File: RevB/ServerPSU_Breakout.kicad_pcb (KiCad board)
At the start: 2 copper layers, 124 x 100 mm, 81 parts, among them J1 Conn_01x05, J2 Conn_01x14, J3 Conn_01x01, J4 Conn_01x01, Q1 DMG2302U, SW1 SW_DIP_x03, SW2 SW_DIP_x04, SW3 SW_DIP_x03, U1 LMR14206, U2 STM32F072RBTx, U3 4051, U4 MIC1555-YM5, U6 MCP1415, U7 AZ1117CR-3.3

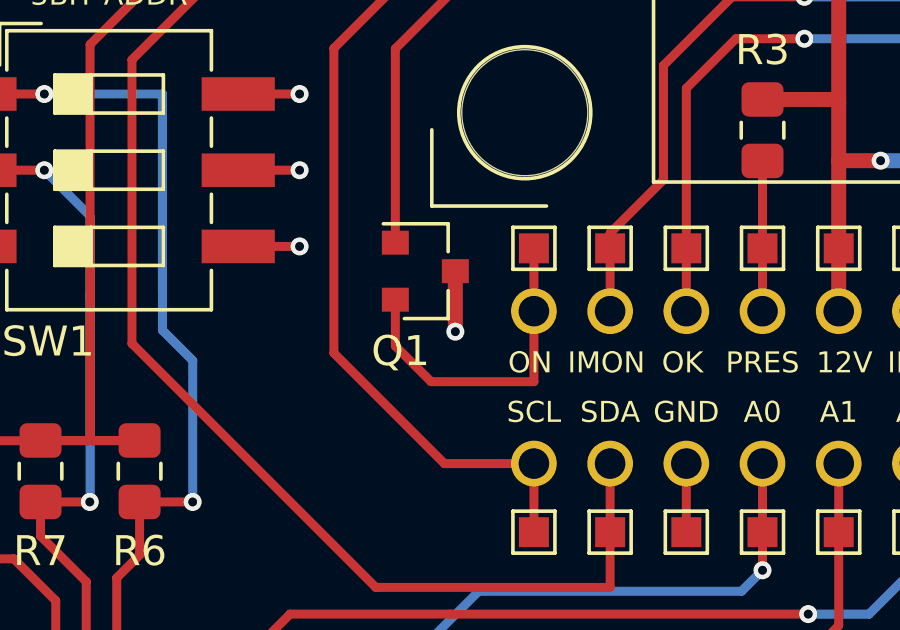
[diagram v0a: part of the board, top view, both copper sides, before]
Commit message: update RevB design
- Corrected PSU_ON n-chan. Drain and Source swapped.
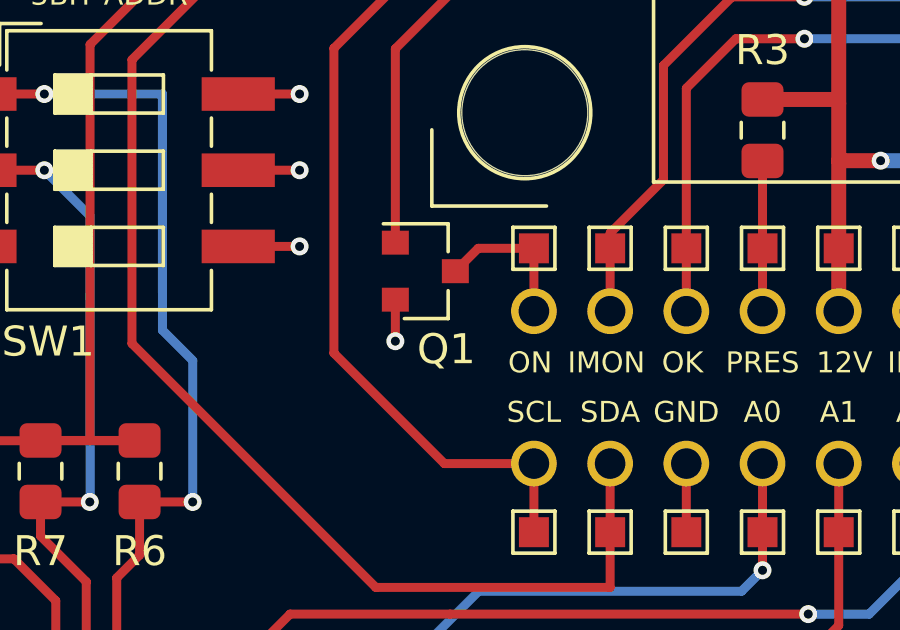
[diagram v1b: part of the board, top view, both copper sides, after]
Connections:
- Q1 pad 2: /HighVoltageControl/PSU_ON -> GNDS
- Q1 pad 3: GNDS -> /HighVoltageControl/PSU_ON
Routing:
- net /HighVoltageControl/PSU_ON: track 11.1 -> 5.03 mm
- net GNDS: track 76.9 -> 76.3 mm

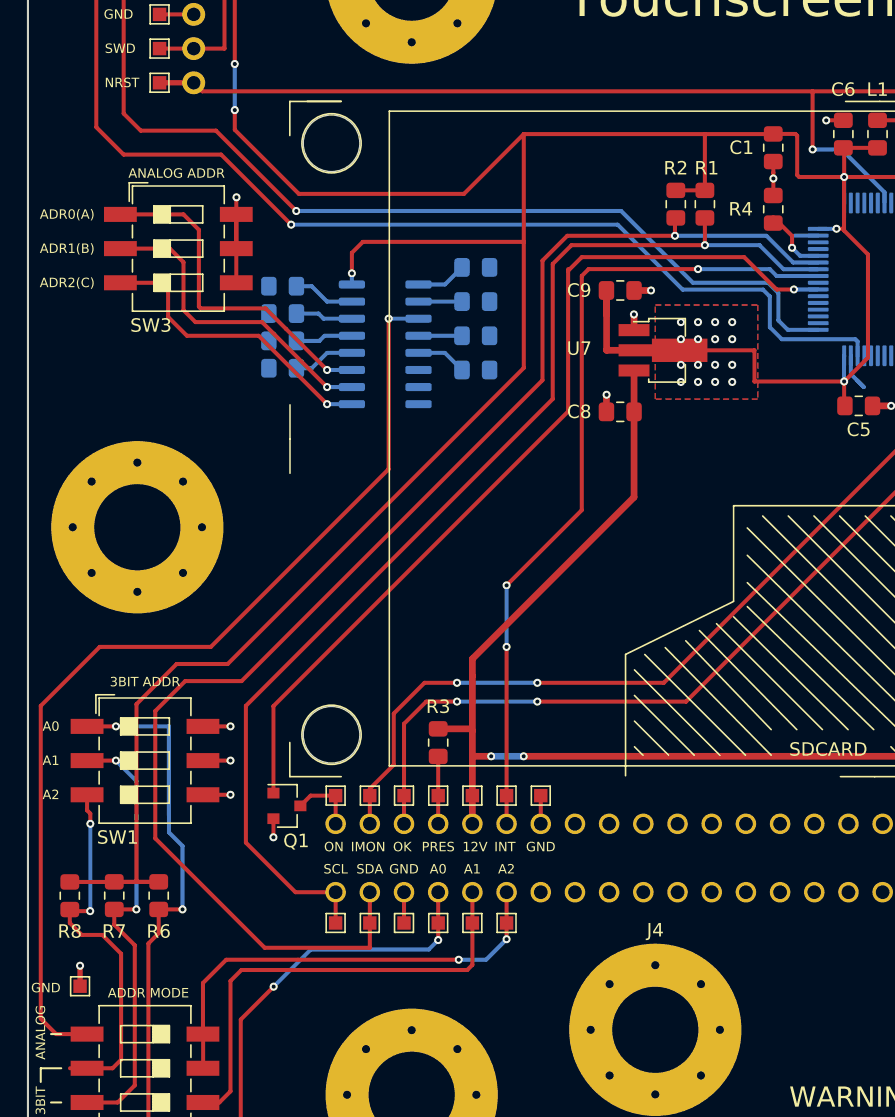
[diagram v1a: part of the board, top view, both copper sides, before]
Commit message: updated revb
added missing pullup resistors
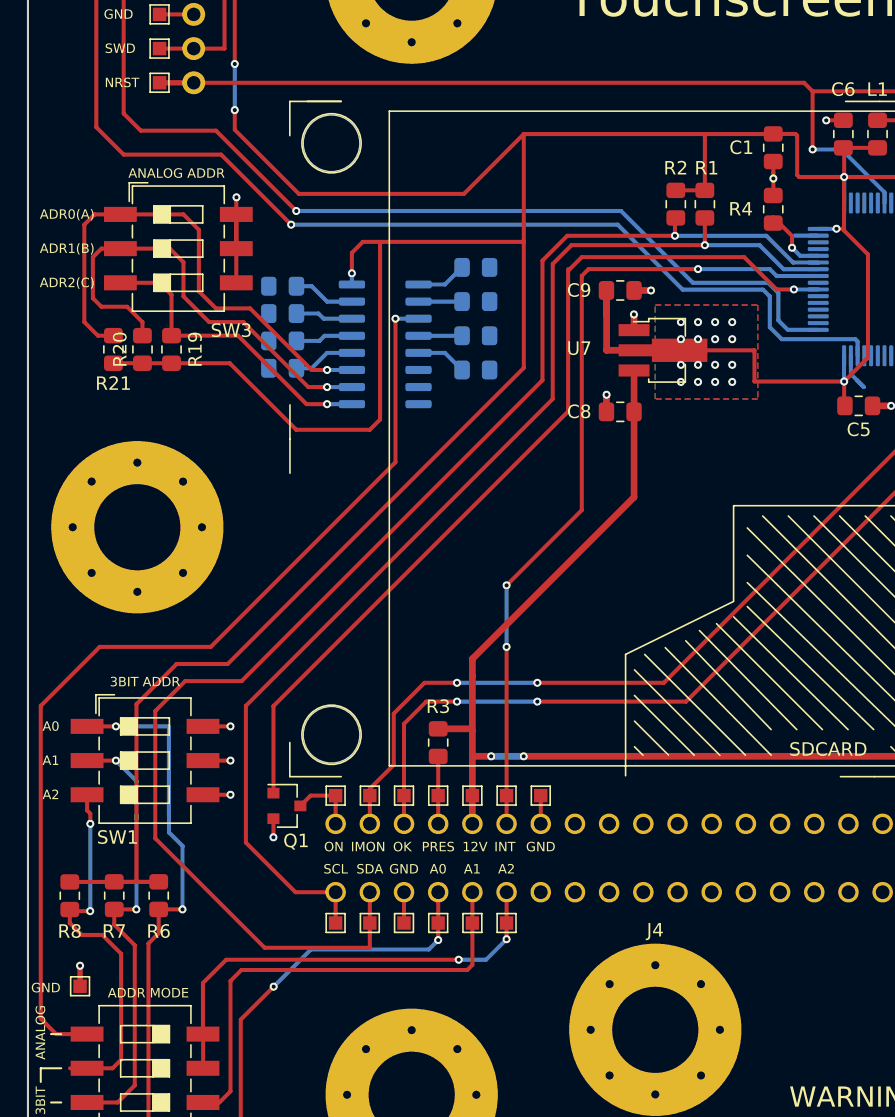
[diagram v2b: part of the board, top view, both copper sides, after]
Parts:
- added R19: 100K, Resistor_SMD:R_0805_2012Metric_Pad1.15x1.40mm_HandSolder, F.Cu at (110.1, 79.5)
- added R20: 100K, Resistor_SMD:R_0805_2012Metric_Pad1.15x1.40mm_HandSolder, F.Cu at (108.0, 79.5)
- added R21: 100K, Resistor_SMD:R_0805_2012Metric_Pad1.15x1.40mm_HandSolder, F.Cu at (105.8, 79.5)
- C11: value 4.7uF X5R 25V -> 1uF X5R 25V
- C14: value 200nF -> 220nF
- C15: value 33uF X5R 10V -> 47uF X5R 10V
- C9: value 100nF -> 330nF
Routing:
- net /HighVoltageControl/MCU_3V3: track 260.7 -> 296.1 mm
- net Net-(R21-Pad2): track 25.3 -> 37.5 mm
- net Net-(R20-Pad2): track 23.5 -> 33.7 mm
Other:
- board text removed: "A"

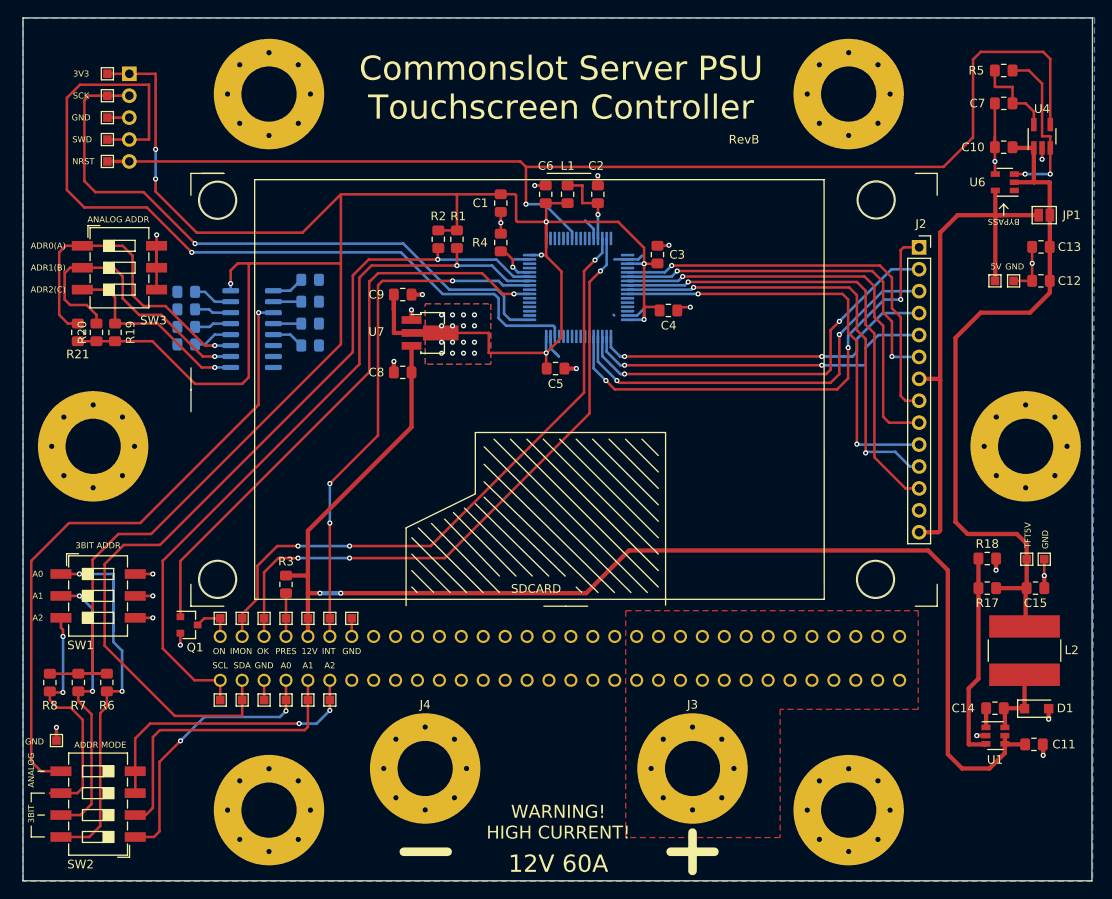
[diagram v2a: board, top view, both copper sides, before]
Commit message: hw update
- Reduced RevB layout dimensions
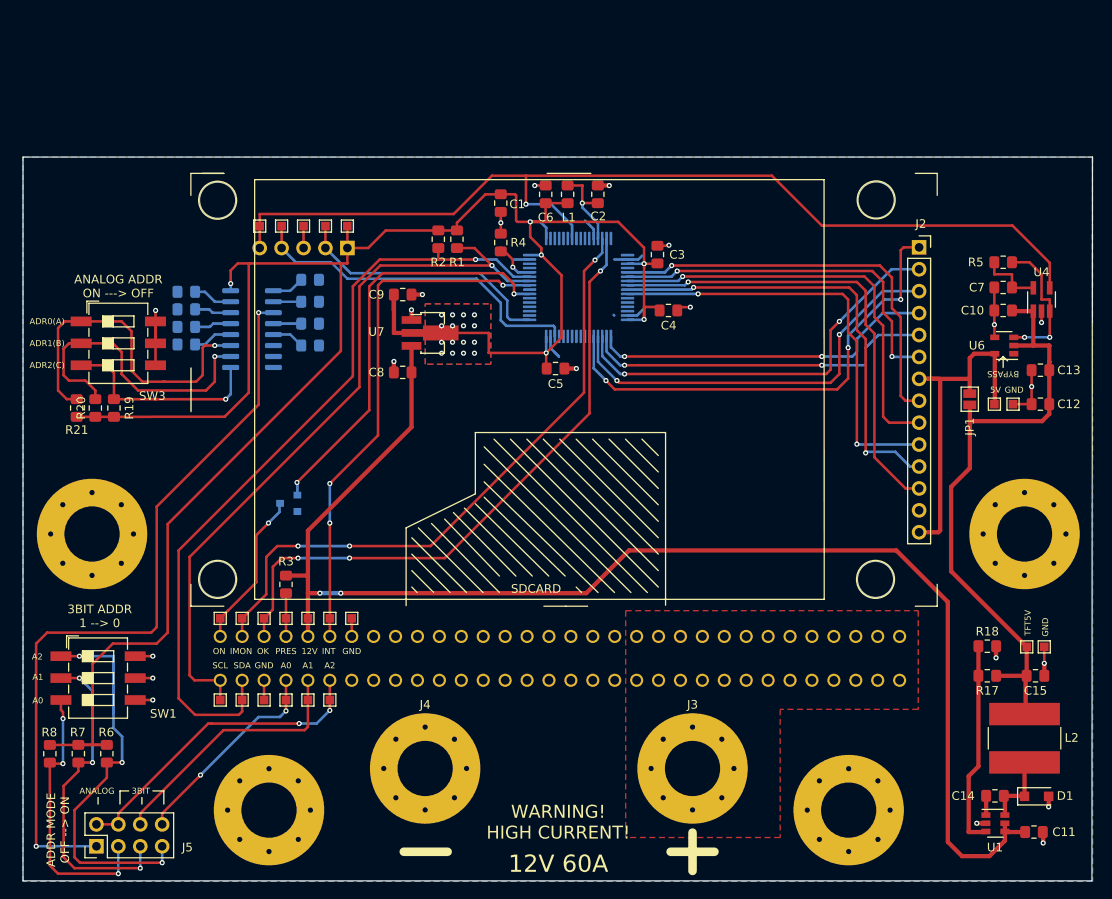
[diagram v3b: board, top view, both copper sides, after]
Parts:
- removed the REF** at (215.6, 92.7)
- removed the REF** at (107.6, 92.7)
- removed the REF** at (195.1, 51.9)
- removed the REF** at (128.0, 51.9)
- removed SW2: SW_DIP_x04, Button_Switch_SMD:SW_DIP_SPSTx04_Slide_6.7x11.72mm_W8.61mm_P2.54mm_LowProfile
- removed TP24: TestPoint, TestPoint:TestPoint_Pad_1.0x1.0mm
- added J5: Conn_02x04_Odd_Even, Connector_PinHeader_2.54mm:PinHeader_2x04_P2.54mm_Vertical, F.Cu at (108.0, 139.1)
- added REF**: MountingHole_6.4mm_M6_Pad_Via, MountingHole:MountingHole_6.4mm_M6_Pad_Via, F.Cu at (215.5, 102.9)
- added REF**: MountingHole_6.4mm_M6_Pad_Via, MountingHole:MountingHole_6.4mm_M6_Pad_Via, F.Cu at (107.4, 102.9)
- Q1: moved to B.Cu
- moved TP1 32.9 mm to (137.0, 67.2), turned to 270 degrees
- moved J1 32.3 mm to (137.0, 69.7), turned to 90 degrees
- moved TP22 29.4 mm to (134.5, 67.2), turned to 270 degrees
- moved TP2 26.0 mm to (132.0, 67.2), turned to 270 degrees
- moved JP1 23.0 mm to (209.2, 87.2), turned to 90 degrees
- moved TP23 22.5 mm to (129.4, 67.2), turned to 270 degrees
- moved R5 22.2 mm to (213.0, 71.4)
- moved C7 21.3 mm to (213.0, 74.3)
- moved TP9 19.2 mm to (126.9, 67.2), turned to 0 degrees
- moved C10 18.9 mm to (213.0, 77.0)
- moved U4 18.9 mm to (217.5, 75.7)
- moved U6 18.9 mm to (213.2, 81.0)
- moved Q1 18.2 mm to (130.2, 99.3), turned to 180 degrees
- moved C12 14.3 mm to (217.4, 87.8)
- moved C13 14.3 mm to (217.4, 83.9)
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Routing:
- net /MCU/SWDIO: track 97.6 -> 40.3 mm, vias 1 -> 0
- net /MCU/SWCLK: track 74.3 -> 30.8 mm, vias 1 -> 0
- net /HighVoltageControl/MCU_3V3: track 296.1 -> 255.0 mm, vias 24 -> 22
- net /MCU/NRST: track 140.1 -> 115.6 mm
- net /MCU/TFT_DelayedReset/TFT_VDD_OUT: track 63.4 -> 41.4 mm
- net /HighVoltageControl/MCU_SW_IN: track 68.1 -> 48.6 mm, vias 1 -> 2
- net Net-(J5-Pad1): track 73.4 -> 88.3 mm, vias 1 -> 2
- net /HighVoltageControl/PSU_ON: track 5.03 -> 18.3 mm, vias 0 -> 1
- net /PSUConnector/PSU_SDA: track 104.2 -> 92.0 mm
- net /MCU/TFTRST_5V: track 80.3 -> 71.9 mm
- net /HighVoltageControl/PSU_12VSB: track 152.0 -> 160.0 mm
- net /PSUConnector/PSU_ADDR0: track 31.8 -> 24.1 mm
- net GNDS: track 76.3 -> 69.9 mm, vias 23 -> 21
- net Net-(J5-Pad5): track 33.5 -> 39.4 mm, vias 2 -> 3
- net /PSUConnector/PSU_ADDR1: track 34.8 -> 30.3 mm
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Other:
- board size 124 x 100 mm -> 124 x 83.9 mm
- board text added: "3BIT ADDR 1 --> 0"
- board text added: "ADDR MODE OFF --> ON"
- board text added: "ANALOG ADDR ON ---> OFF"
- board text removed: "3BIT ADDR"
- board text removed: "3V3"
- board text removed: "ADDR MODE"
- board text removed: "ANALOG ADDR"
- board text removed: "NRST"
- board text removed: "SCK"
- board text removed: "SWD"

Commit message: hw update
- changed third dip switch to cd4066 and spdt slide switch
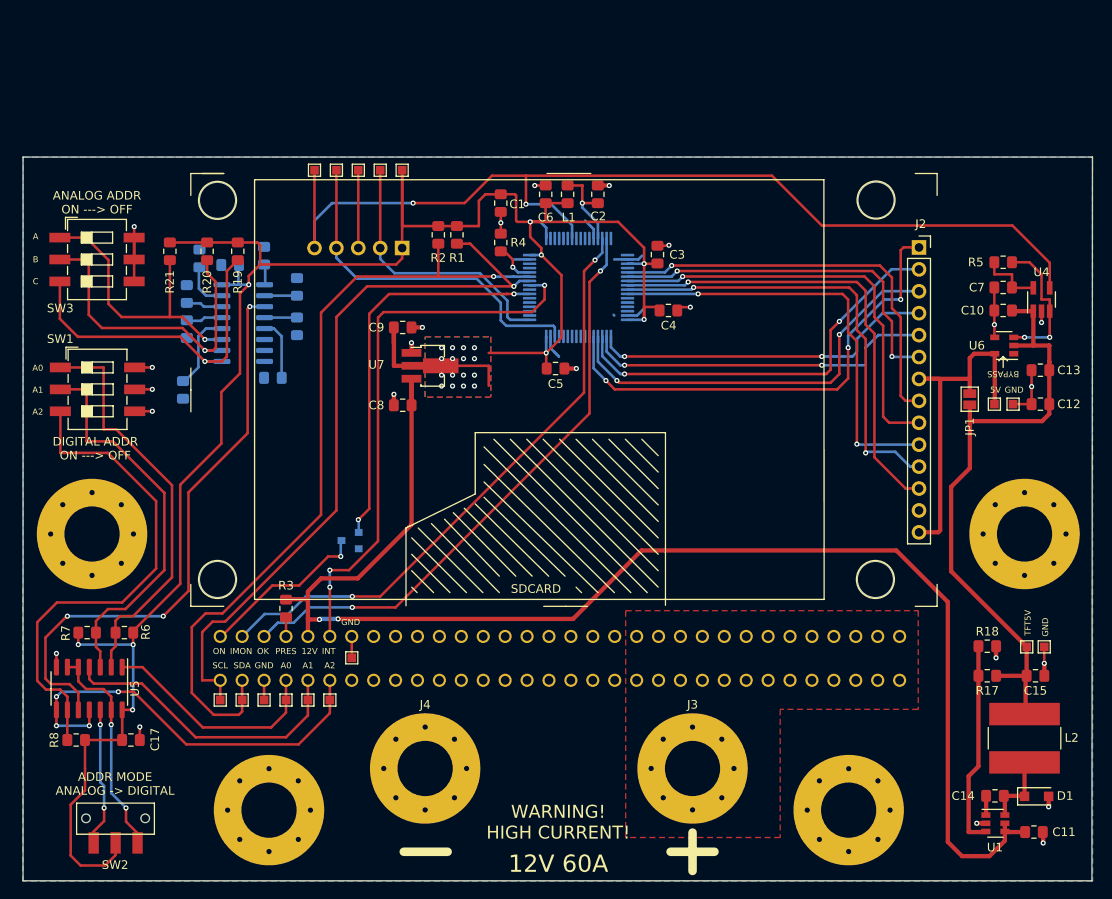
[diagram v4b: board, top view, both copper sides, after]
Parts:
- removed J5: Conn_02x04_Odd_Even, Connector_PinHeader_2.54mm:PinHeader_2x04_P2.54mm_Vertical
- removed TP17, TP18, TP19, TP20, TP21, TP4: TestPoint, TestPoint:TestPoint_Pad_1.0x1.0mm
- added C16: 100nF, Capacitor_SMD:C_0805_2012Metric_Pad1.15x1.40mm_HandSolder, B.Cu at (123.4, 71.7)
- added C17: 100nF, Capacitor_SMD:C_0805_2012Metric_Pad1.15x1.40mm_HandSolder, F.Cu at (112.0, 126.7)
- added SW2: SW_SPDT, JS_Series_Sub-Miniature_Slide_Switches:JS102011SAQN, F.Cu at (110.2, 137.4)
- added U5: 4066, Package_SO:SOIC-14_3.9x8.7mm_P1.27mm, F.Cu at (107.1, 120.8)
- moved SW1 33.5 mm to (108.1, 86.1)
- moved R19 23.1 mm to (124.3, 70.1), turned to 270 degrees
- moved R20 22.3 mm to (120.8, 70.1), turned to 270 degrees
- moved R21 21.1 mm to (116.5, 70.1), turned to 270 degrees
- moved R6 14.2 mm to (111.2, 114.3), turned to 180 degrees
- moved R7 14.1 mm to (106.9, 114.3), turned to 0 degrees
- moved SW3 10.0 mm to (108.0, 71.1)
- moved TP1 9.07 mm to (143.4, 60.7)
- moved TP9 9.07 mm to (133.2, 60.7)
- moved TP2 9.07 mm to (138.3, 60.7)
- moved TP22 9.07 mm to (140.8, 60.7)
- moved TP23 9.07 mm to (135.8, 60.7)
- moved Q1 8.32 mm to (137.4, 103.6)
- moved J1 6.35 mm to (143.4, 69.7)
- moved R13 6.02 mm to (127.4, 70.6), turned to 90 degrees
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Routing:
- net Net-(R8-Pad2): track 32.4 -> 58.5 mm, vias 3 -> 0
- net /MCU/SMBUS_Addressing/ENABLE_DIGITAL: track 0.00 -> 25.7 mm, vias 0 -> 2
- net Net-(U3-Pad3): track 88.3 -> 67.6 mm, vias 2 -> 3
- net /MCU/SMBUS_Addressing/ENABLE_ANALOG: track 0.00 -> 16.1 mm, vias 0 -> 2
- net Net-(R19-Pad2): track 24.5 -> 39.8 mm
- net /PSUConnector/PSU_ADDR2: track 36.8 -> 48.8 mm, vias 2 -> 4
- net GNDS: track 69.9 -> 79.8 mm, vias 21 -> 23
- net Net-(R21-Pad2): track 39.4 -> 33.2 mm
- net Net-(R7-Pad2): track 39.4 -> 45.4 mm, vias 3 -> 0
- net /HighVoltageControl/MCU_3V3: track 255.0 -> 259.6 mm, vias 22 -> 25
- net Net-(R12-Pad1): track 4.59 -> 9.05 mm
- net /PSUConnector/PSU_ADDR1: track 30.3 -> 34.6 mm
- net Net-(R6-Pad2): track 52.1 -> 47.7 mm, vias 3 -> 0
- net /MCU/MCU_PSOK: track 73.7 -> 69.5 mm, vias 3 -> 2
- net /MCU/MCU_IMON: track 73.8 -> 70.1 mm, vias 3 -> 2
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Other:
- board text added: "A"
- board text added: "ADDR MODE ANALOG -> DIGITAL"
- board text added: "B"
- board text added: "C"
- board text added: "DIGITAL ADDR ON ---> OFF"
- board text removed: "3BIT"
- board text removed: "3BIT ADDR 1 --> 0"
- board text removed: "ADDR MODE OFF --> ON"
- board text removed: "ADR0(A)"
- board text removed: "ADR1(B)"
- board text removed: "ADR2(C)"
- board text removed: "ANALOG"
